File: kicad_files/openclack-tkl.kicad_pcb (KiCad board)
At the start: 2 copper layers, 345.7 x 134.1 mm, 206 parts, among them CON1 USB-MINI-B, Q1 60V 1.2A, SW0:0 ESC, SW0:10 F9, SW0:11 F10, SW0:12 F11, SW0:13 F12, SW0:14 PRINT, SW0:15 SCROLL LOCK, SW0:2 F1, SW0:3 F2, SW0:4 F3, SW0:5 F4, SW0:6 F5, SW0:7 F6, SW0:8 F7, SW0:9 F8, SW1:0 `, SW1:1 1, SW1:10 0, SW1:11 -, SW1:12 =, SW1:13 BACK SPACE, SW1:14 INSERT, SW1:15 HOME, SW1:2 2, SW1:3 3, SW1:4 4, SW1:5 5, SW1:6 6, SW1:7 7, SW1:8 8, SW1:9 9, SW2:0 TAB, SW2:1 Q, SW2:10 P, SW2:11 [, SW2:12 ], SW2:13 \, SW2:14 DELETE, SW2:15 END, SW2:2 W, SW2:3 E, SW2:4 R, SW2:5 T, SW2:6 Y, SW2:7 U, SW2:8 I, SW2:9 O, SW3:0 CAPS LOCK, SW3:1 A, SW3:10 ;, SW3:11 ', SW3:13 ENTER, SW3:14 PAGE UP, SW3:15 PAUSE, SW3:2 S, SW3:3 D, SW3:4 F, SW3:5 G, SW3:6 H, SW3:7 J, SW3:8 K, SW3:9 L, SW4:0 LEFT SHIFT, SW4:1 Z, SW4:10 /, SW4:13 RIGHT SHIFT, SW4:14 PAGE DOWN, SW4:15 UP, SW4:2 X, SW4:3 C, SW4:4 V, SW4:5 B, SW4:6 N, SW4:7 M, SW4:8 ,, SW4:9 ., SW5:0 LEFT CTRL, SW5:1 LEFT WINDOWS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

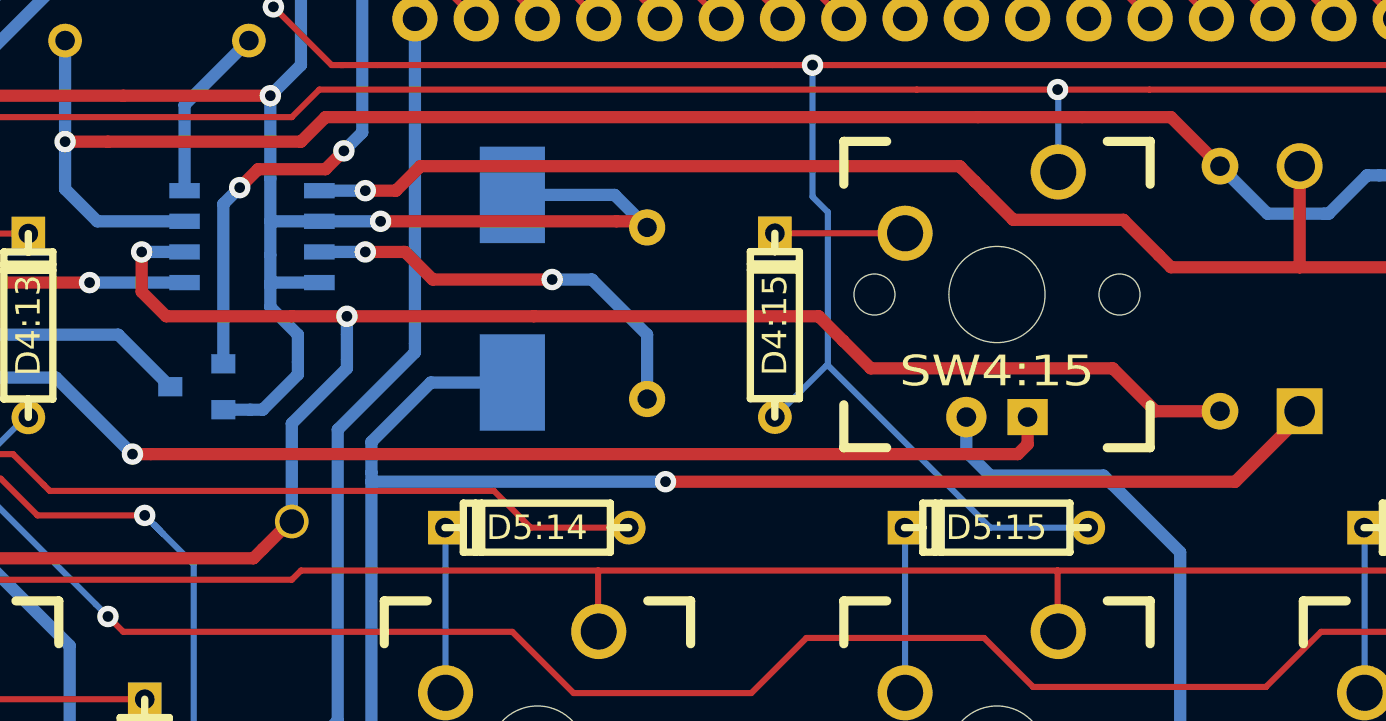
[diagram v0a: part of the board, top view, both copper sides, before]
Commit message: Increased pad distance for BC CT1, prototype was a tight fit.
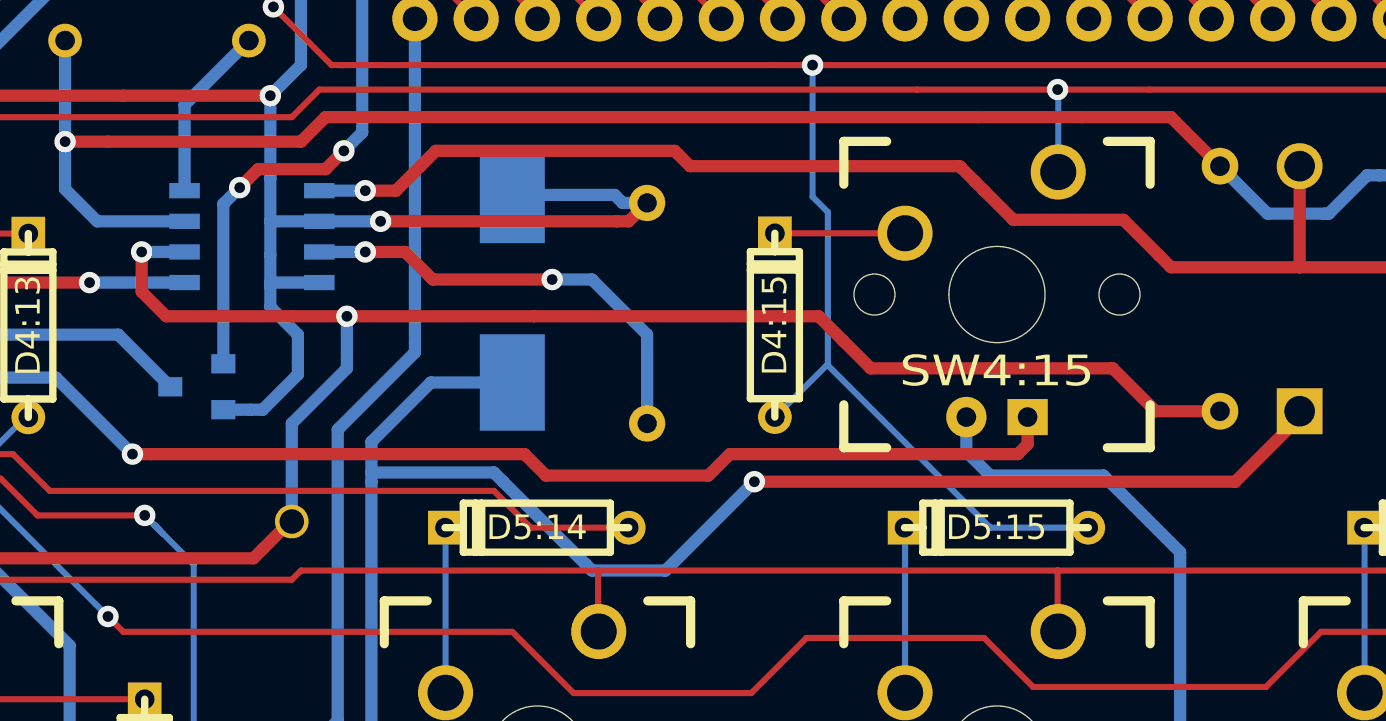
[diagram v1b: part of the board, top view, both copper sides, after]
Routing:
- net /LEDCOL0: track 731.6 -> 734.8 mm
- net N-00000112: track 17.7 -> 18.7 mm
- net N-0000092: track 140.4 -> 141.2 mm
- net N-00000107: track 59.5 -> 60.0 mm
